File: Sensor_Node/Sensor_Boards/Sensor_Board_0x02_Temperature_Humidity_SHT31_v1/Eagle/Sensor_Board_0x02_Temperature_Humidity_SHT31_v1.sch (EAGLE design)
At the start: 16 parts, among them J1 M04_SMD_90, J4 ARDUINO_ISP, U2 ATMEGA328P_TQFP, Y1 8MHZ

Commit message: SHT31
- reset path
- sensor connector footer
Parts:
- removed U$20: M08_SMD_STRAIGHT, myownthings:M08_SMD_STRAIGHT
- added U$9: M08_SMD_STRAIGHT, wsn:M08_SMD_STRAIGHT
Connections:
- removed net N$4: C1.2, R5.1, S1.RIGHT, U2.PC6(/RESET)
- new net FTDI_RESET: C1.1, SV1.6
- net GND: now also U$9.7; no longer U$20.7
- net RESET: now also C1.2, R5.1, S1.RIGHT, U2.PC6(/RESET); no longer C1.1, SV1.6
- net SCL: now also U$9.6; no longer U$20.6
- net SDA: now also U$9.5; no longer U$20.5
- net VCC: now also U$9.8; no longer U$20.8

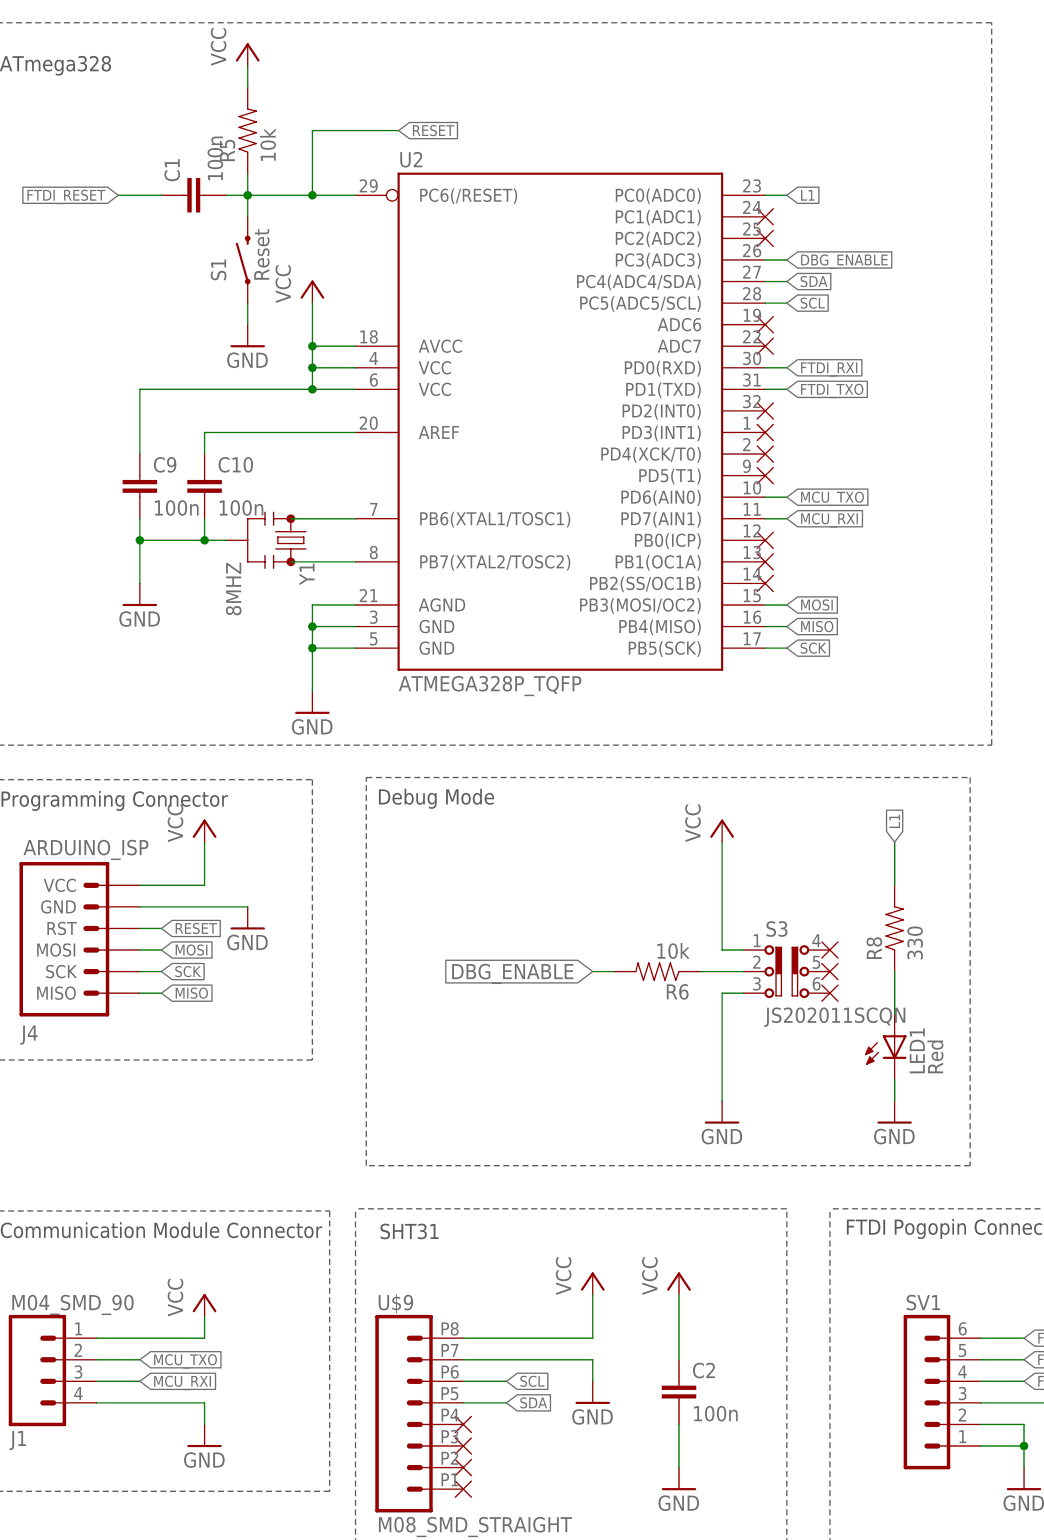
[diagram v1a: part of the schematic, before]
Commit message: Update SHT31
- only descriptions missing
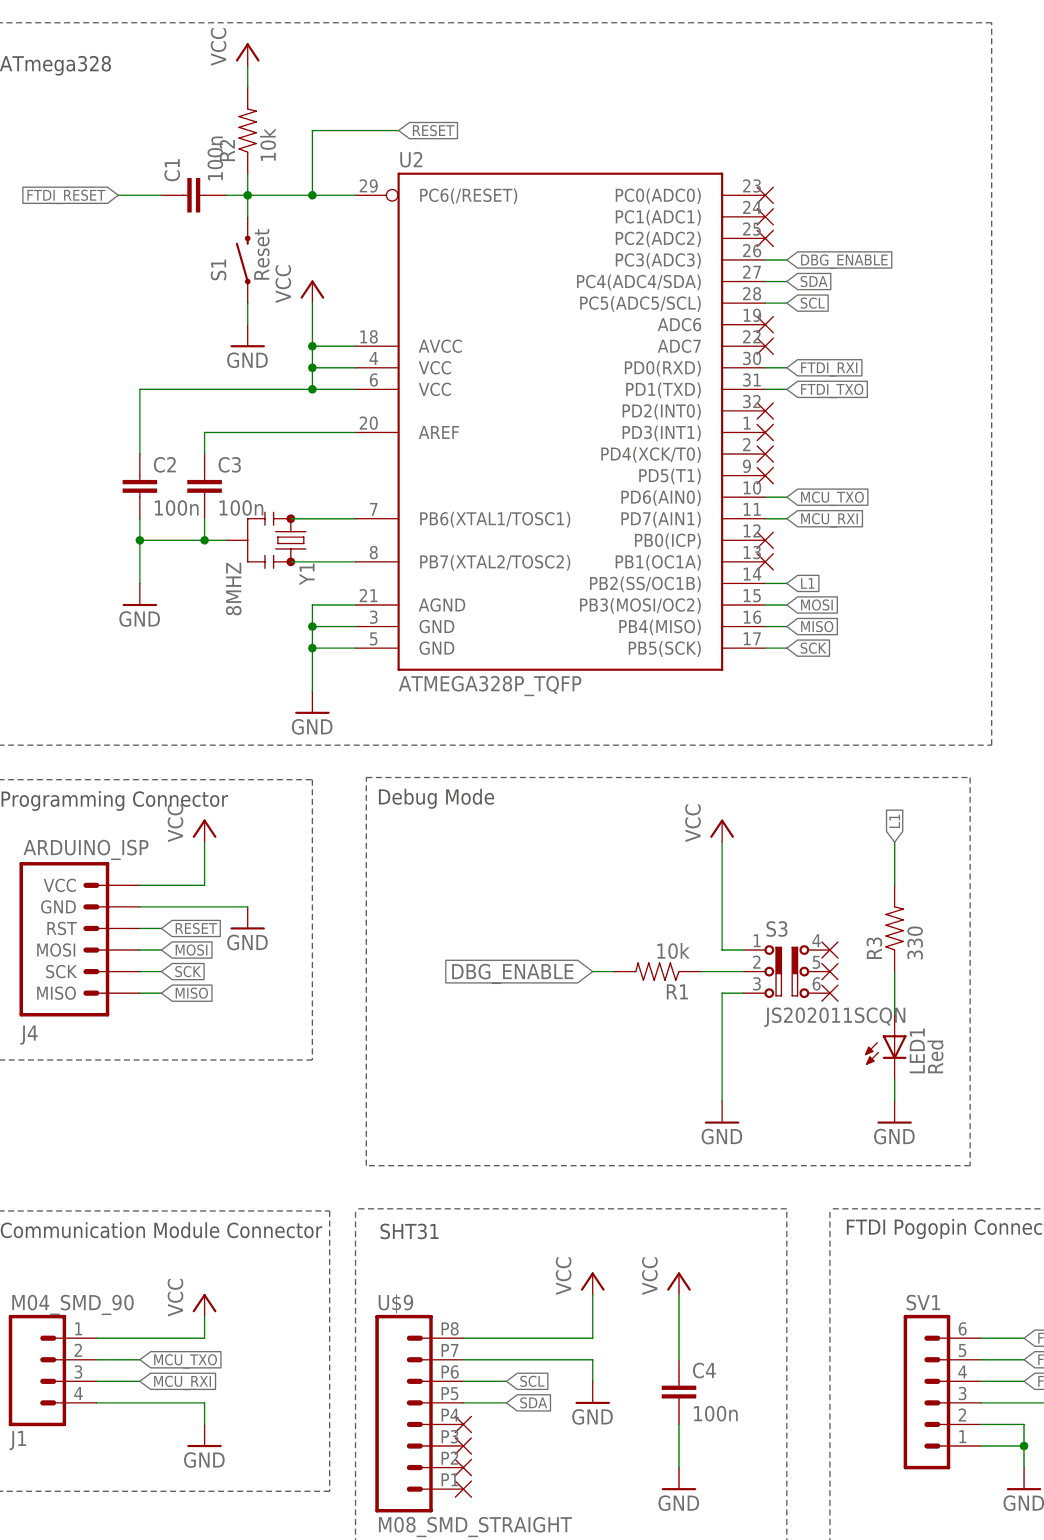
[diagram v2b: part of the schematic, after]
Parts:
- removed C9: 100n, eagle-ltspice:C
- added C4: 100n, eagle-ltspice:C
- renumbered C10 to C3, R5 to R2, R6 to R1, R8 to R3
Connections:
- net GND: now also C4.2; no longer C9.2
- net L1: now also U2.PB2(SS/OC1B); no longer U2.PC0(ADC0)
- net VCC: now also C4.1; no longer C9.1
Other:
- moved on the sheet: C2
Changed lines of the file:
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@@
 <?xml version="1.0" encoding="utf-8"?>
 <!DOCTYPE eagle SYSTEM "eagle.dtd">
-<eagle version="8.2.2">
+<eagle version="8.4.2">
 <drawing>
 <settings>
 <setting alwaysvectorfont="no"/>
+<setting keepoldvectorfont="yes"/>
 <setting verticaltext="up"/>
 </settings>
@@
 <part name="GND16" library="SparkFun" deviceset="GND" device=""/>
 <part name="GND18" library="SparkFun" deviceset="GND" device=""/>
-<part name="R5" library="SparkFun-Passives" deviceset="RESISTOR" device="0805-RES" value="10k"/>
-<part name="C10" library="eagle-ltspice" deviceset="C" device="" value="100n"/>
+<part name="R2" library="SparkFun-Passives" deviceset="RESISTOR" device="0805-RES" value="10k"/>
+<part name="C3" library="eagle-ltspice" deviceset="C" device="" value="100n"/>
 <part name="GND5" library="SparkFun-Aesthetics" deviceset="GND" device=""/>
 <part name="LED1" library="led" deviceset="LED" device="SML0805" value="Red"/>
-<part name="R8" library="SparkFun-Passives" deviceset="RESISTOR" device="0805-RES" value="330"/>
+<part name="R3" library="SparkFun-Passives" deviceset="RESISTOR" device="0805-RES" value="330"/>
 <part name="GND20" library="SparkFun-Aesthetics" deviceset="GND" device=""/>
-<part name="C9" library="eagle-ltspice" deviceset="C" device="" value="100n"/>
-<part name="R6" library="SparkFun-Passives" deviceset="RESISTOR" device="0805-RES" value="10k"/>
+<part name="C2" library="eagle-ltspice" deviceset="C" device="" value="100n"/>
+<part name="R1" library="SparkFun-Passives" deviceset="RESISTOR" device="0805-RES" value="10k"/>
 <part name="GND19" library="SparkFun" deviceset="GND" device=""/>
 <part name="U2" library="marc_library" deviceset="ATMEGA328P_TQFP" device="" value="ATMEGA328P_TQFP"/>
@@
 <part name="GND2" library="SparkFun-Aesthetics" deviceset="GND" device=""/>
 <part name="GND7" library="supply1" deviceset="GND" device=""/>
-<part name="C2" library="eagle-ltspice" deviceset="C" device="" value="100n"/>
+<part name="C4" library="eagle-ltspice" deviceset="C" device="" value="100n"/>
 <part name="GND9" library="SparkFun" deviceset="GND" device=""/>
 <part name="P+1" library="supply1" deviceset="VCC" device=""/>
@@
 <part name="U$11" library="myownthings" deviceset="N/C" device=""/>
 <part name="U$12" library="myownthings" deviceset="N/C" device=""/>
-<part name="U$13" library="myownthings" deviceset="N/C" device=""/>
 <part name="U$14" library="myownthings" deviceset="N/C" device=""/>
 <part name="U$15" library="myownthings" deviceset="N/C" device=""/>
@@
 <part name="U$2" library="myownthings" deviceset="N/C" device=""/>
 <part name="U$9" library="wsn" deviceset="M08_SMD_STRAIGHT" device=""/>
+<part name="U$10" library="myownthings" deviceset="N/C" device=""/>
 </parts>
 <sheets>
@@
 <instance part="GND16" gate="1" x="25.4" y="134.62"/>
 <instance part="GND18" gate="1" x="45.72" y="121.92"/>
-<instance part="R5" gate="G$1" x="38.1" y="190.5" rot="R90"/>
-<instance part="C10" gate="G$1" x="33.02" y="149.86"/>
+<instance part="R2" gate="G$1" x="38.1" y="190.5" rot="R90"/>
+<instance part="C3" gate="G$1" x="33.02" y="149.86"/>
 <instance part="GND5" gate="1" x="38.1" y="96.52"/>
 <instance part="LED1" gate="G$1" x="114.3" y="83.82"/>
-<instance part="R8" gate="G$1" x="114.3" y="96.52" rot="R90"/>
+<instance part="R3" gate="G$1" x="114.3" y="96.52" rot="R90"/>
 <instance part="GND20" gate="1" x="114.3" y="73.66"/>
-<instance part="C9" gate="G$1" x="25.4" y="149.86"/>
-<instance part="R6" gate="G$1" x="86.36" y="91.44" rot="R180"/>
+<instance part="C2" gate="G$1" x="25.4" y="149.86"/>
+<instance part="R1" gate="G$1" x="86.36" y="91.44" rot="R180"/>
 <instance part="GND19" gate="1" x="93.98" y="73.66"/>
 <instance part="U2" gate="U$1" x="55.88" y="127"/>
@@
 <instance part="GND2" gate="1" x="33.02" y="35.56"/>
 <instance part="GND7" gate="1" x="78.74" y="40.64"/>
-<instance part="C2" gate="G$1" x="88.9" y="43.18"/>
+<instance part="C4" gate="G$1" x="88.9" y="43.18"/>
 <instance part="GND9" gate="1" x="88.9" y="30.48"/>
 <instance part="P+1" gate="VCC" x="38.1" y="200.66"/>
@@
 <instance part="U$11" gate="G$1" x="99.06" y="142.24"/>
 <instance part="U$12" gate="G$1" x="99.06" y="139.7"/>
-<instance part="U$13" gate="G$1" x="99.06" y="137.16"/>
 <instance part="U$14" gate="G$1" x="106.68" y="93.98"/>
 <instance part="U$15" gate="G$1" x="106.68" y="91.44"/>
@@
 <instance part="U$2" gate="G$1" x="99.06" y="177.8"/>
 <instance part="U$9" gate="G$1" x="58.42" y="35.56"/>
+<instance part="U$10" gate="G$1" x="99.06" y="182.88"/>
 </instances>
 <busses>
@@
 <pinref part="GND16" gate="1" pin="GND"/>
 <wire x1="25.4" y1="137.16" x2="25.4" y2="142.24" width="0.1524" layer="91"/>
-<pinref part="C10" gate="G$1" pin="2"/>
+<pinref part="C3" gate="G$1" pin="2"/>
 <wire x1="33.02" y1="144.78" x2="33.02" y2="142.24" width="0.1524" layer="91"/>
 <junction x="33.02" y="142.24"/>
-<pinref part="C9" gate="G$1" pin="2"/>
+<pinref part="C2" gate="G$1" pin="2"/>
 <wire x1="25.4" y1="142.24" x2="25.4" y2="144.78" width="0.1524" layer="91"/>
 <junction x="25.4" y="142.24"/>
@@
 <segment>
 <pinref part="GND9" gate="1" pin="GND"/>
-<pinref part="C2" gate="G$1" pin="2"/>
+<pinref part="C4" gate="G$1" pin="2"/>
 <wire x1="88.9" y1="33.02" x2="88.9" y2="38.1" width="0.1524" layer="91"/>
 </segment>
@@
 <wire x1="45.72" y1="160.02" x2="25.4" y2="160.02" width="0.1524" layer="91"/>
 <junction x="45.72" y="160.02"/>
-<pinref part="C9" gate="G$1" pin="1"/>
+<pinref part="C2" gate="G$1" pin="1"/>
 <wire x1="25.4" y1="152.4" x2="25.4" y2="160.02" width="0.1524" layer="91"/>
 <pinref part="P+2" gate="VCC" pin="VCC"/>
@@
 </segment>
 <segment>
-<pinref part="R5" gate="G$1" pin="2"/>
+<pinref part="R2" gate="G$1" pin="2"/>
 <pinref part="P+1" gate="VCC" pin="VCC"/>
 <wire x1="38.1" y1="198.12" x2="38.1" y2="195.58" width="0.1524" layer="91"/>
 </segment>
 <segment>
-<pinref part="C2" gate="G$1" pin="1"/>
+<pinref part="C4" gate="G$1" pin="1"/>
 <wire x1="88.9" y1="53.34" x2="88.9" y2="45.72" width="0.1524" layer="91"/>
 <pinref part="P+15" gate="VCC" pin="VCC"/>
@@
 </segment>
 <segment>
-<pinref part="R5" gate="G$1" pin="1"/>
+<pinref part="R2" gate="G$1" pin="1"/>
 <pinref part="S1" gate="G$1" pin="RIGHT"/>
 <wire x1="38.1" y1="185.42" x2="38.1" y2="182.88" width="0.1524" layer="91"/>
@@
 <net name="L1" class="0">
 <segment>
-<pinref part="R8" gate="G$1" pin="2"/>
+<pinref part="R3" gate="G$1" pin="2"/>
 <wire x1="114.3" y1="101.6" x2="114.3" y2="106.68" width="0.1524" layer="91"/>
 <label x="114.3" y="106.68" size="1.27" layer="95" rot="R90" xref="yes"/>
 </segment>
 <segment>
-<wire x1="99.06" y1="182.88" x2="101.6" y2="182.88" width="0.1524" layer="91"/>
-<label x="101.6" y="182.88" size="1.27" layer="95" xref="yes"/>
-<pinref part="U2" gate="U$1" pin="PC0(ADC0)"/>
+<pinref part="U2" gate="U$1" pin="PB2(SS/OC1B)"/>
+<wire x1="99.06" y1="137.16" x2="101.6" y2="137.16" width="0.1524" layer="91"/>
+<label x="101.6" y="137.16" size="1.27" layer="95" xref="yes"/>
 </segment>
 </net>
@@
 </segment>
 <segment>
-<pinref part="R6" gate="G$1" pin="2"/>
+<pinref part="R1" gate="G$1" pin="2"/>
 <wire x1="81.28" y1="91.44" x2="78.74" y2="91.44" width="0.1524" layer="91"/>
 <label x="78.74" y="91.44" size="1.778" layer="95" rot="R180" xref="yes"/>
@@
 <segment>
 <pinref part="LED1" gate="G$1" pin="A"/>
-<pinref part="R8" gate="G$1" pin="1"/>
+<pinref part="R3" gate="G$1" pin="1"/>
 <wire x1="114.3" y1="86.36" x2="114.3" y2="91.44" width="0.1524" layer="91"/>
 </segment>
@@
 <net name="N$15" class="0">
 <segment>
-<pinref part="C10" gate="G$1" pin="1"/>
+<pinref part="C3" gate="G$1" pin="1"/>
 <pinref part="U2" gate="U$1" pin="AREF"/>
 <wire x1="33.02" y1="152.4" x2="33.02" y2="154.94" width="0.1524" layer="91"/>
@@
 <segment>
 <pinref part="S3" gate="G$1" pin="2"/>
-<pinref part="R6" gate="G$1" pin="1"/>
+<pinref part="R1" gate="G$1" pin="1"/>
 <wire x1="96.52" y1="91.44" x2="91.44" y2="91.44" width="0.1524" layer="91"/>
 </segment>
